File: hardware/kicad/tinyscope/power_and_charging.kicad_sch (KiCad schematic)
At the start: 45 parts, among them SW2 SW_SPST

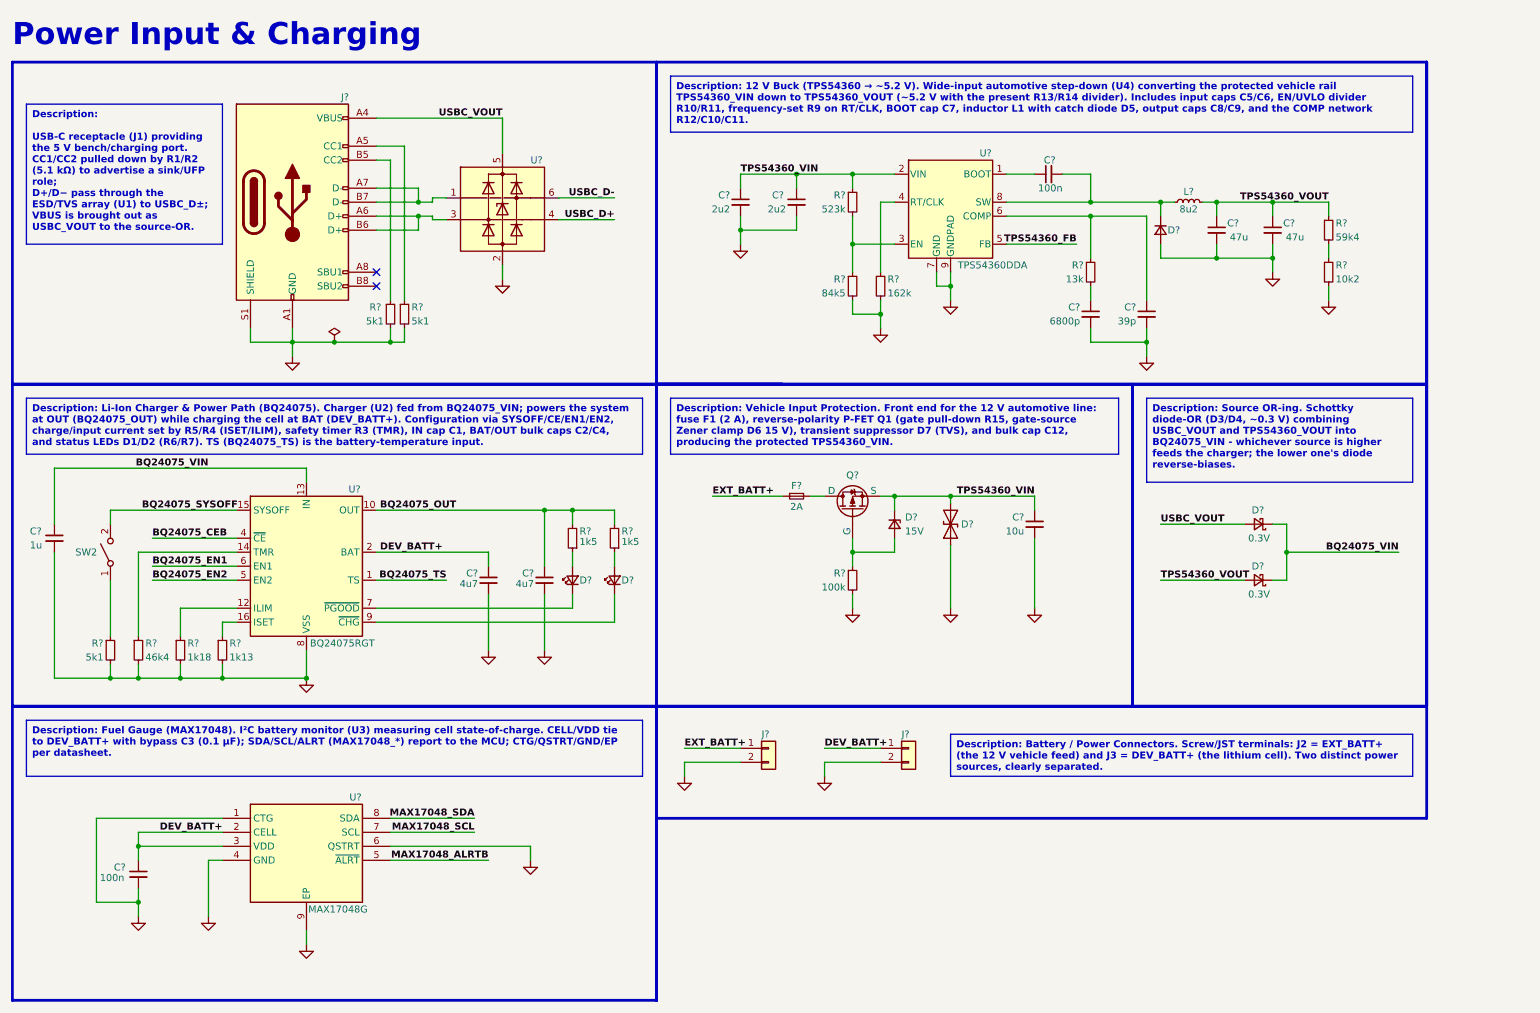
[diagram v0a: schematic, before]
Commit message: feat: hardware: Adds Waveshare 16498 display 02x17 connector. Cleans up all schematics
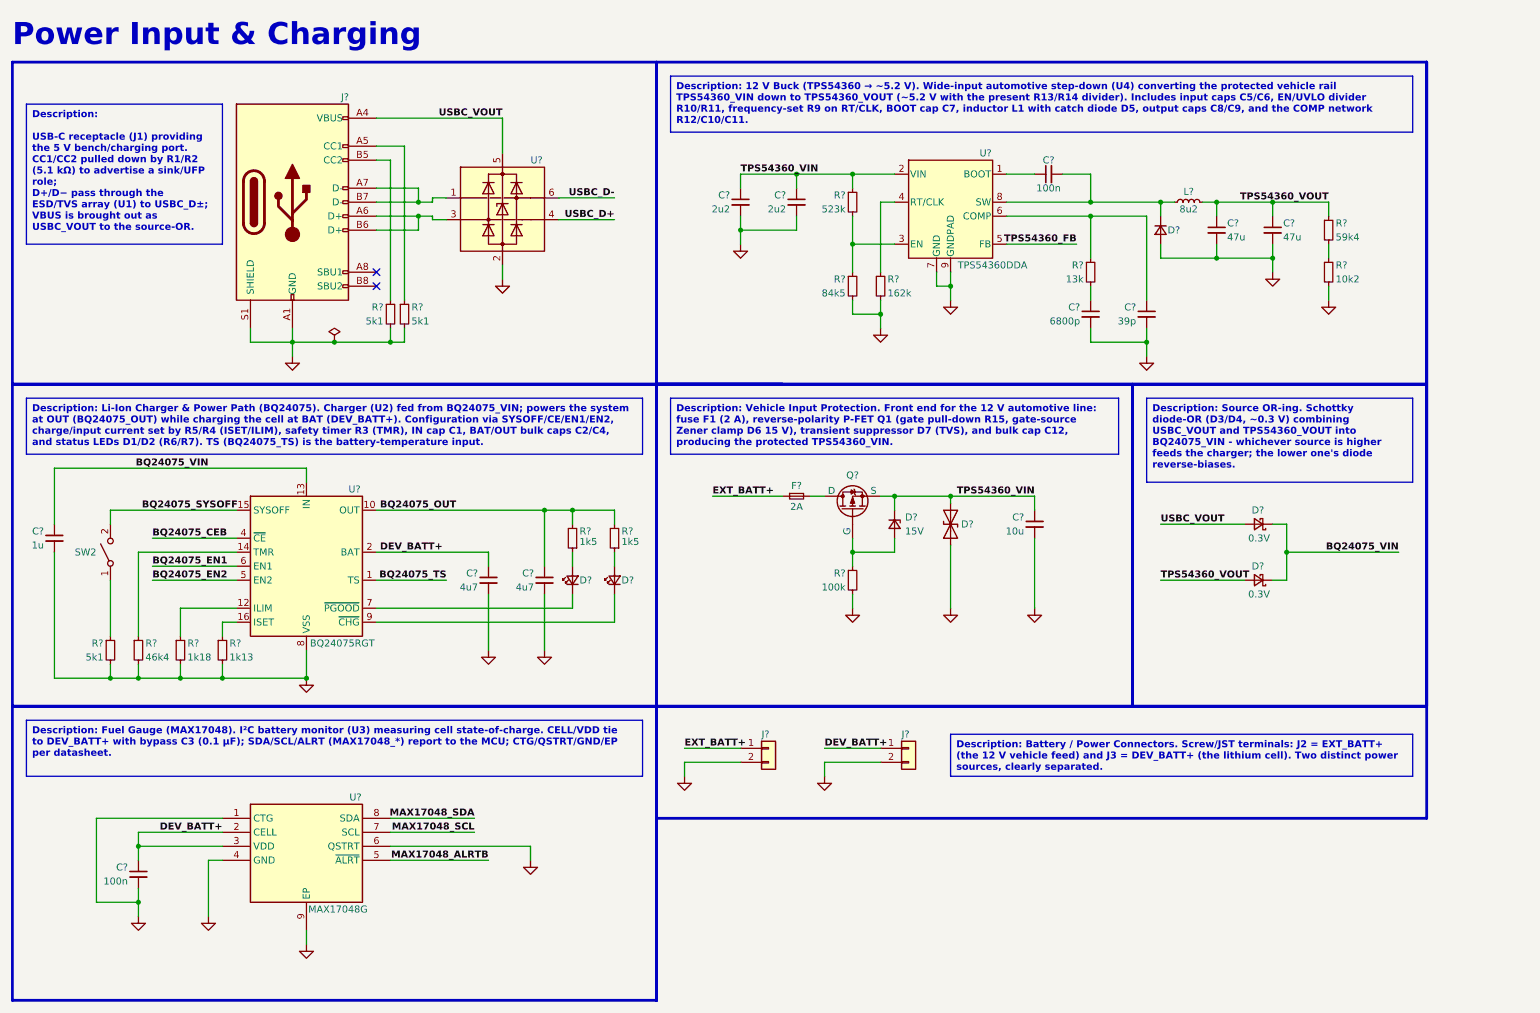
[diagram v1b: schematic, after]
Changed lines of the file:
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@@
   (symbol (lib_id "Device:C_Small") (at 208.28 43.18 90) (unit 1)
     (in_bom yes) (on_board yes) (dnp no)
-    (property "Reference" "C?" (at 209.55 40.64 90)
-      (effects (font (size 1.27 1.27)) (justify left))
-    )
-    (property "Value" "100n" (at 206.375 45.72 90)
-      (effects (font (size 1.27 1.27)) (justify right))
+    (property "Reference" "C?" (at 208.28 40.64 90)
+      (effects (font (size 1.27 1.27)))
+    )
+    (property "Value" "100n" (at 208.28 45.72 90)
+      (effects (font (size 1.27 1.27)))
     )
     (property "Footprint" "" (at 208.28 43.18 0)
@@
   (symbol (lib_id "Device:C_Small") (at 162.56 48.26 0) (unit 1)
     (in_bom yes) (on_board yes) (dnp no)
-    (property "Reference" "C?" (at 158.115 46.99 0)
-      (effects (font (size 1.27 1.27)) (justify left))
+    (property "Reference" "C?" (at 160.655 46.99 0)
+      (effects (font (size 1.27 1.27)) (justify right))
     )
     (property "Value" "2u2" (at 160.655 49.53 0)
@@
       (effects (font (size 1.27 1.27)) (justify right))
     )
-    (property "Value" "4u7" (at 104.775 117.475 0)
+    (property "Value" "4u7" (at 104.775 118.11 0)
       (effects (font (size 1.27 1.27)) (justify right))
     )
@@
   (symbol (lib_id "Switch:SW_SPST") (at 38.1 111.76 90) (unit 1)
     (in_bom yes) (on_board yes) (dnp no)
-    (property "Reference" "SW2" (at 31.75 111.76 90)
-      (effects (font (size 1.27 1.27)) (justify right))
+    (property "Reference" "SW2" (at 35.56 111.76 90)
+      (effects (font (size 1.27 1.27)) (justify left))
     )
     (property "Value" "SW_SPST" (at 39.37 113.03 90)
@@
   (symbol (lib_id "Device:C_Small") (at 43.18 170.18 0) (unit 1)
     (in_bom yes) (on_board yes) (dnp no)
-    (property "Reference" "C?" (at 38.735 168.91 0)
-      (effects (font (size 1.27 1.27)) (justify left))
-    )
-    (property "Value" "100n" (at 36.195 170.815 0)
-      (effects (font (size 1.27 1.27)) (justify left))
+    (property "Reference" "C?" (at 41.275 168.91 0)
+      (effects (font (size 1.27 1.27)) (justify right))
+    )
+    (property "Value" "100n" (at 41.275 171.45 0)
+      (effects (font (size 1.27 1.27)) (justify right))
     )
     (property "Footprint" "" (at 43.18 170.18 0)
@@
   (symbol (lib_id "Device:C_Small") (at 27.94 109.22 0) (unit 1)
     (in_bom yes) (on_board yes) (dnp no)
-    (property "Reference" "C?" (at 23.495 107.95 0)
-      (effects (font (size 1.27 1.27)) (justify left))
-    )
-    (property "Value" "1u" (at 23.495 110.49 0)
-      (effects (font (size 1.27 1.27)) (justify left))
+    (property "Reference" "C?" (at 26.035 107.95 0)
+      (effects (font (size 1.27 1.27)) (justify right))
+    )
+    (property "Value" "1u" (at 26.035 110.49 0)
+      (effects (font (size 1.27 1.27)) (justify right))
     )
     (property "Footprint" "" (at 27.94 109.22 0)
@@
       (effects (font (size 1.27 1.27)) (justify left))
     )
-    (property "Value" "47u" (at 254.635 54.61 0)
-      (effects (font (size 1.27 1.27)) (justify right))
+    (property "Value" "47u" (at 250.825 54.61 0)
+      (effects (font (size 1.27 1.27)) (justify left))
     )
     (property "Footprint" "" (at 248.92 53.34 0)
@@
       (effects (font (size 1.27 1.27)) (justify left))
     )
-    (property "Value" "47u" (at 244.475 54.61 0)
-      (effects (font (size 1.27 1.27)) (justify right))
+    (property "Value" "47u" (at 240.665 54.61 0)
+      (effects (font (size 1.27 1.27)) (justify left))
     )
     (property "Footprint" "" (at 238.76 53.34 0)
@@
   (symbol (lib_id "Device:R_Small") (at 88.9 68.58 0) (unit 1)
     (in_bom yes) (on_board yes) (dnp no)
-    (property "Reference" "R?" (at 85.09 67.31 0)
-      (effects (font (size 1.27 1.27)) (justify left))
-    )
-    (property "Value" "5k1" (at 84.455 69.85 0)
-      (effects (font (size 1.27 1.27)) (justify left))
+    (property "Reference" "R?" (at 87.63 67.31 0)
+      (effects (font (size 1.27 1.27)) (justify right))
+    )
+    (property "Value" "5k1" (at 87.63 69.85 0)
+      (effects (font (size 1.27 1.27)) (justify right))
     )
     (property "Footprint" "" (at 88.9 68.58 0)
@@
       (effects (font (size 1.27 1.27)) (justify right))
     )
-    (property "Value" "4u7" (at 114.935 117.475 0)
-      (effects (font (size 1.27 1.27)) (justify right))
-    )
+    (property "Value" "4u7" (at 114.935 118.11 0)
+      (effects (font (size 1.27 1.27)) (justify right))
+    )

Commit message: fix: hardware: Solves electrical rules warnings and errors #1
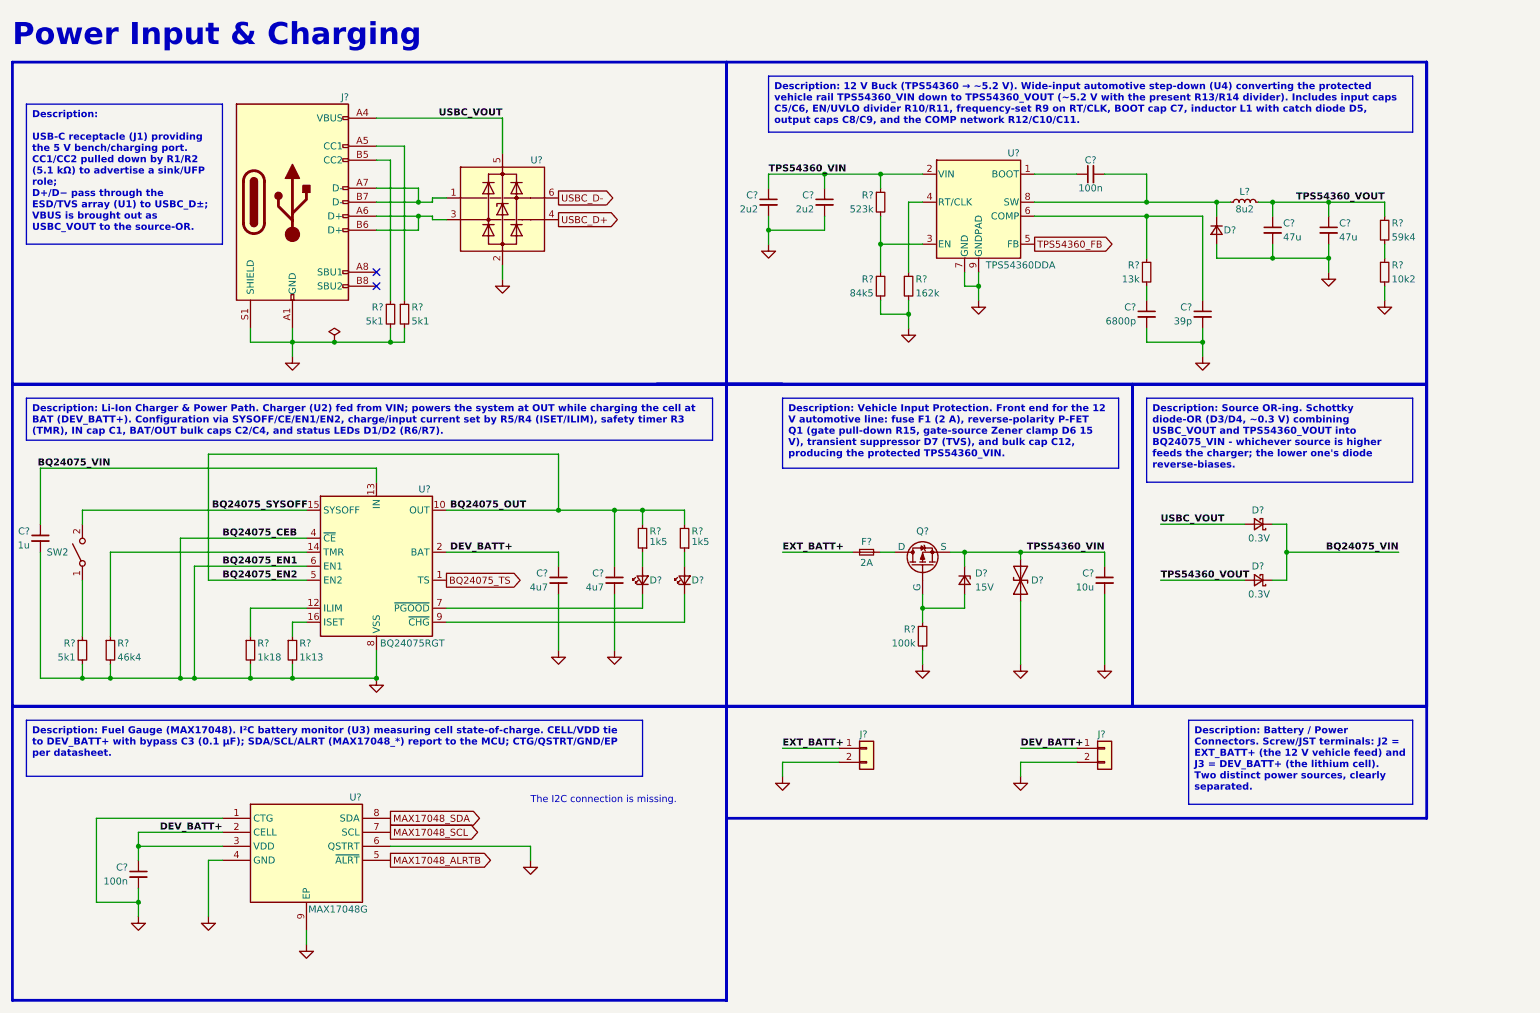
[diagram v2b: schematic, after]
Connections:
- net BQ24075_CEB is gone; now on net GND: U?.4 (~{CE})
- net BQ24075_EN1 is gone; now on net GND: U?.6 (EN1)
- net BQ24075_OUT is gone; now on net BQ24075_EN2: C?.1, R?.2, R?.2, U?.10 (OUT), U?.11 (OUT)
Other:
- note added: "The I2C connection is missing."
- moved on the sheet: C?, D?, F?, J?, L?, Q?, R?, SW2, U?

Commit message: fix: hardware: Solves electrical rules warnings and errors #3
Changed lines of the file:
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@@
     (effects (font (size 1.27 1.27) bold) (justify left bottom))
   )
-  (global_label "TPS54360_FB" (shape output) (at 205.74 55.88 0) (fields_autoplaced)
+  (global_label "TPS54360_FB" (shape bidirectional) (at 205.74 55.88 0) (fields_autoplaced)
     (effects (font (size 1.27 1.27)) (justify left))
-    (property "Intersheetrefs" "${INTERSHEET_REFS}" (at 221.4666 55.88 0)
+    (property "Intersheetrefs" "${INTERSHEET_REFS}" (at 222.5779 55.88 0)
       (effects (font (size 1.27 1.27)) (justify left) hide)
     )
   )
-  (global_label "MAX17048_SDA" (shape output) (at 88.9 160.02 0) (fields_autoplaced)
+  (global_label "MAX17048_SDA" (shape bidirectional) (at 88.9 160.02 0) (fields_autoplaced)
     (effects (font (size 1.27 1.27)) (justify left))
-    (property "Intersheetrefs" "${INTERSHEET_REFS}" (at 106.1385 160.02 0)
+    (property "Intersheetrefs" "${INTERSHEET_REFS}" (at 107.2498 160.02 0)
       (effects (font (size 1.27 1.27)) (justify left) hide)
     )
   )
-  (global_label "USBC_D+" (shape output) (at 119.38 51.435 0) (fields_autoplaced)
+  (global_label "USBC_D+" (shape bidirectional) (at 119.38 51.435 0) (fields_autoplaced)
     (effects (font (size 1.27 1.27)) (justify left))
-    (property "Intersheetrefs" "${INTERSHEET_REFS}" (at 131.1758 51.435 0)
+    (property "Intersheetrefs" "${INTERSHEET_REFS}" (at 132.2871 51.435 0)
       (effects (font (size 1.27 1.27)) (justify left) hide)
     )
   )
-  (global_label "BQ24075_TS" (shape output) (at 99.06 116.84 0) (fields_autoplaced)
+  (global_label "BQ24075_TS" (shape bidirectional) (at 99.06 116.84 0) (fields_autoplaced)
     (effects (font (size 1.27 1.27)) (justify left))
-    (property "Intersheetrefs" "${INTERSHEET_REFS}" (at 113.7585 116.84 0)
+    (property "Intersheetrefs" "${INTERSHEET_REFS}" (at 114.8698 116.84 0)
       (effects (font (size 1.27 1.27)) (justify left) hide)
     )
   )
-  (global_label "USBC_D-" (shape output) (at 119.38 47.498 0) (fields_autoplaced)
+  (global_label "USBC_D-" (shape bidirectional) (at 119.38 47.498 0) (fields_autoplaced)
     (effects (font (size 1.27 1.27)) (justify left))
-    (property "Intersheetrefs" "${INTERSHEET_REFS}" (at 131.1758 47.498 0)
+    (property "Intersheetrefs" "${INTERSHEET_REFS}" (at 132.2871 47.498 0)
       (effects (font (size 1.27 1.27)) (justify left) hide)
     )
   )
-  (global_label "MAX17048_ALRTB" (shape output) (at 88.9 167.64 0) (fields_autoplaced)
+  (global_label "MAX17048_ALRTB" (shape bidirectional) (at 88.9 167.64 0) (fields_autoplaced)
     (effects (font (size 1.27 1.27)) (justify left))
-    (property "Intersheetrefs" "${INTERSHEET_REFS}" (at 108.1947 167.64 0)
+    (property "Intersheetrefs" "${INTERSHEET_REFS}" (at 109.306 167.64 0)
       (effects (font (size 1.27 1.27)) (justify left) hide)
     )
   )
-  (global_label "MAX17048_SCL" (shape output) (at 88.9 162.56 0) (fields_autoplaced)
+  (global_label "MAX17048_SCL" (shape bidirectional) (at 88.9 162.56 0) (fields_autoplaced)
     (effects (font (size 1.27 1.27)) (justify left))
-    (property "Intersheetrefs" "${INTERSHEET_REFS}" (at 106.078 162.56 0)
+    (property "Intersheetrefs" "${INTERSHEET_REFS}" (at 107.1893 162.56 0)
       (effects (font (size 1.27 1.27)) (justify left) hide)
     )

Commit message: feat: hardware: Add global labels on power and charging, and regulation and rails subschematics
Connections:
- net BQ24075_EN2 renamed BQ24075_OUT
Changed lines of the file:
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@@
-    (effects (font (size 1.27 1.27) bold) (justify left bottom))
-  )
-  (label "BQ24075_OUT" (at 99.695 104.14 0) (fields_autoplaced)
     (effects (font (size 1.27 1.27) bold) (justify left bottom))
   )
@@
       (effects (font (size 1.27 1.27)) (justify left) hide)
     )
+  )
+  (global_label "BQ24075_OUT" (shape bidirectional) (at 119.38 93.98 0) (fields_autoplaced)
+    (effects (font (size 1.27 1.27)) (justify left))
+    (property "Intersheetrefs" "${INTERSHEET_REFS}" (at 136.6413 93.98 0)
+      (effects (font (size 1.27 1.27)) (justify left) hide)
+    )

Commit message: fix: hardware: Solves electrical rules warnings and errors #7
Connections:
- net TPS54360_FB is gone; now on an unnamed net: U?.5 (FB)
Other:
- moved on the sheet: C?, R?
